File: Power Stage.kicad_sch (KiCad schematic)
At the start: 25 parts, among them J3 Screw_Terminal_01x01, Q10 HYG017N10NS1TA, Q13 HYG017N10NS1TA, Q3 HYG017N10NS1TA, Q6 HYG017N10NS1TA, U3 IRS21867S, U8 CSA231MA

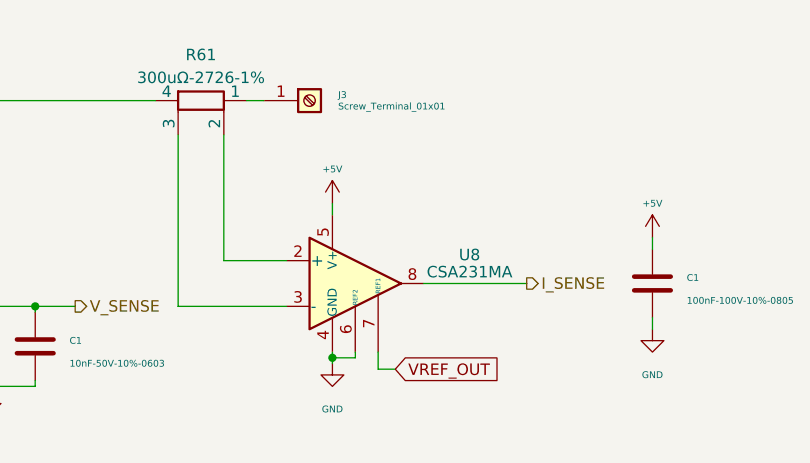
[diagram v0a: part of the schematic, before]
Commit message: Done with first pass, switching current amp due to stocking issues
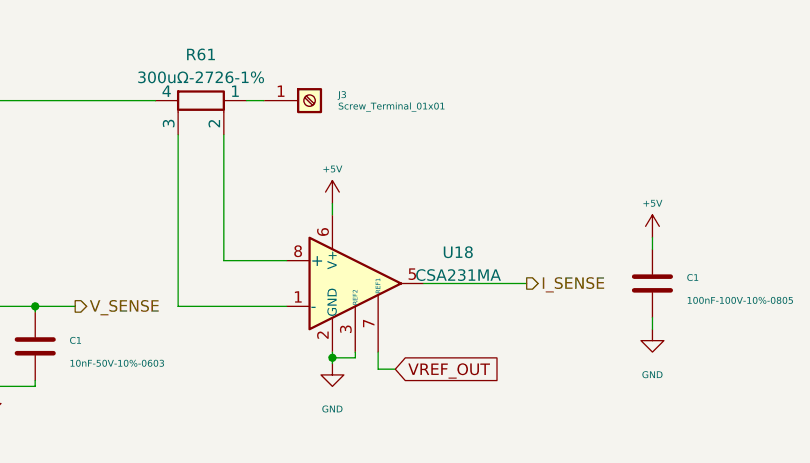
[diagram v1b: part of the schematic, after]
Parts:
- removed U8: CSA231MA, Package_SO:TSSOP-8_4.4x3mm_P0.65mm, symbol Amplifier_Current:INA240A1PW
- added U18: CSA231MA, Package_SO:SOIC-8_3.9x4.9mm_P1.27mm, symbol Amplifier_Current:INA240A1D
- C1: MPN (none) -> C28233
- C1: MPN (none) -> C2843466
- C1: MPN (none) -> C57112
- C1: MPN (none) -> C13832
- D1: MPN (none) -> C14996
- Q10, Q13, Q3, Q6: MPN (none) -> C5205219
- R11: MPN (none) -> C5159707
- R11: MPN (none) -> C149504
- R11: MPN (none) -> C22859
- R61: LCSC (none) -> C481539; MPN (none) -> C481539
- U3: MPN (none) -> C7432820
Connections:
- net +5V: now also U18.6 (V+)
- net GND: now also U18.2 (GND), U18.3 (REF2), U18.4 (GND)
- net I_SENSE: now also U18.5
- net VREF_OUT: now also U18.7 (REF1)
- net at R61.2: now also U18.8 (+)
- net at R61.3: now also U18.1 (-)
